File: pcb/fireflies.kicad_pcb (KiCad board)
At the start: 2 copper layers, 58 x 26.5 mm, 51 parts, among them J1 USB_C_Receptacle_USB2.0_14P, J2 Flash, Q1 AO3416, Q2 AO3416, Q3 AO3416, SW1 SW_Push, SW2 SW_Push, U1 YD3622ARL, U2 CH32V003FxUx, U3 LTR-303ALS-01, U4 XT1861, U5 XC6206PxxxMR

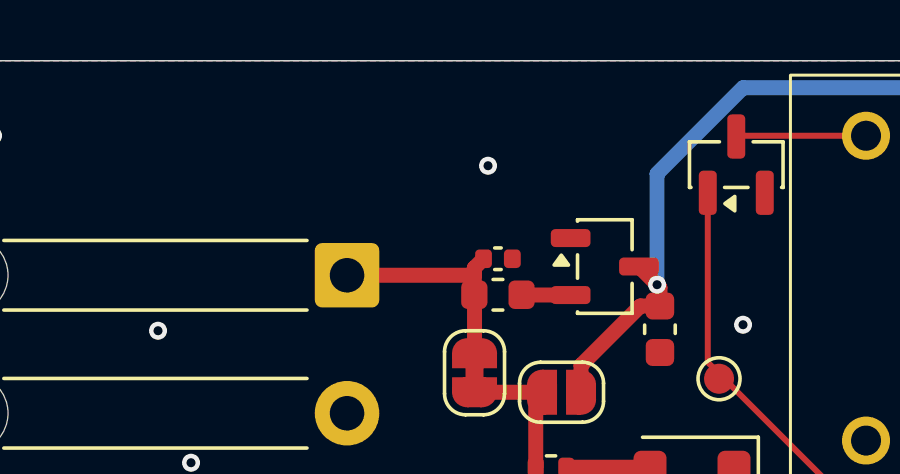
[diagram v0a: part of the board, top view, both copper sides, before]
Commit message: Hardware i2c stub
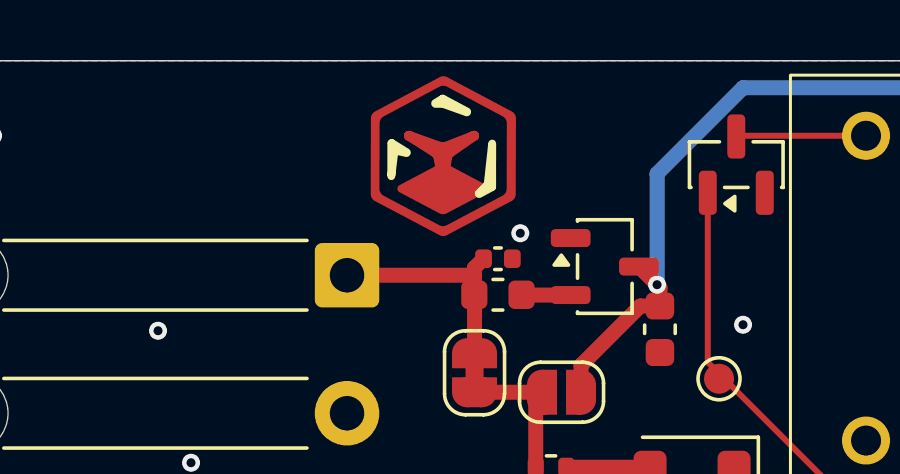
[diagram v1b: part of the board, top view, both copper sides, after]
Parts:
- added REF**: Icy Electronics Logo, Mainboard:Icy Electronics Logo, F.Cu at (103.0, 80.2)
